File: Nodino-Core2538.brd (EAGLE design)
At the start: 27.9 x 25.4 mm, 21 parts, among them CON1 NODINO-JTAGMODULE, CON2 USB-OTG_SHIELD, IC1 CC2538, IC2 AP733333SAG, Q1 32MHz, Q2 32.768kHz

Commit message: final version, but still missing A0-A5 and AREF
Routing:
- net +3V3: track 83.3 -> 88.6 mm
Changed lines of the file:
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@@
 <via x="8.128" y="15.3035" extent="1-16" drill="0.3302"/>
 <wire x1="9.144" y1="9.0805" x2="10.3505" y2="10.287" width="0.2032" layer="16"/>
-<wire x1="10.3505" y1="10.287" x2="10.3505" y2="11.8745" width="0.2032" layer="16"/>
 <via x="10.414" y="11.938" extent="1-16" drill="0.3302"/>
 <wire x1="12.153384375" y1="12.278528125" x2="11.7954125" y2="12.6365" width="0.2032" layer="1"/>
 <wire x1="11.7954125" y1="12.6365" x2="11.1125" y2="12.6365" width="0.2032" layer="1"/>
 <wire x1="11.1125" y1="12.6365" x2="10.414" y2="11.938" width="0.2032" layer="1"/>
-<wire x1="10.3505" y1="11.8745" x2="10.414" y2="11.938" width="0.2032" layer="16"/>
 <wire x1="5.7785" y1="15.3035" x2="8.128" y2="15.3035" width="0.2032" layer="16"/>
 <wire x1="18.161" y1="17.526" x2="12.573" y2="11.938" width="0.2032" layer="16"/>
@@
 <wire x1="16.58466875" y1="16.52116875" x2="17.5895" y2="17.526" width="0.2032" layer="1"/>
 <wire x1="17.5895" y1="17.526" x2="18.2245" y2="17.526" width="0.2032" layer="1"/>
-<wire x1="6.096" y1="13.589" x2="5.2705" y2="12.7635" width="0.2032" layer="16"/>
+<wire x1="6.1595" y1="13.6525" x2="5.2705" y2="12.7635" width="0.2032" layer="16"/>
 <wire x1="5.2705" y1="12.7635" x2="4.2545" y2="12.7635" width="0.2032" layer="16"/>
 <wire x1="4.2545" y1="12.7635" x2="3.7465" y2="13.2715" width="0.2032" layer="16"/>
@@
 <wire x1="7.278" y1="15.152" x2="7.4295" y2="15.3035" width="0.2032" layer="1"/>
 <wire x1="7.4295" y1="15.3035" x2="8.128" y2="15.3035" width="0.2032" layer="1"/>
-<wire x1="10.414" y1="11.938" x2="7.278" y2="14.351" width="0" layer="19" extent="1-1"/>
+<wire x1="10.3505" y1="10.287" x2="10.3505" y2="11.049" width="0.2032" layer="16"/>
+<wire x1="10.3505" y1="11.049" x2="10.0965" y2="11.303" width="0.2032" layer="16"/>
+<wire x1="10.414" y1="11.938" x2="10.0965" y2="11.6205" width="0.2032" layer="16"/>
+<wire x1="10.0965" y1="11.6205" x2="10.0965" y2="11.303" width="0.2032" layer="16"/>
+<wire x1="10.414" y1="11.938" x2="9.652" y2="12.7" width="0.2032" layer="16"/>
+<wire x1="9.652" y1="12.7" x2="9.0805" y2="12.7" width="0.2032" layer="16"/>
+<wire x1="9.0805" y1="12.7" x2="8.128" y2="13.6525" width="0.2032" layer="16"/>
+<wire x1="8.128" y1="13.6525" x2="6.1595" y2="13.6525" width="0.2032" layer="16"/>
 </signal>
 <signal name="CS2">
@@
 <contactref element="IC1" pad="2"/>
 <via x="6.0325" y="9.652" extent="1-16" drill="0.3302"/>
-<via x="9.398" y="10.922" extent="1-16" drill="0.3302"/>
+<via x="9.5885" y="10.922" extent="1-16" drill="0.3302"/>
 <wire x1="11.604915625" y1="9.9695" x2="12.153384375" y2="10.58146875" width="0.2032" layer="1"/>
 <wire x1="11.604915625" y1="9.9695" x2="10.795" y2="9.9695" width="0.2032" layer="1"/>
@@
 <wire x1="5.2705" y1="8.89" x2="6.0325" y2="9.652" width="0.2032" layer="1"/>
 <wire x1="6.0325" y1="9.652" x2="7.3025" y2="10.922" width="0.2032" layer="16"/>
-<wire x1="7.3025" y1="10.922" x2="9.398" y2="10.922" width="0.2032" layer="16"/>
-<wire x1="9.398" y1="10.922" x2="9.8425" y2="10.922" width="0.2032" layer="1"/>
+<wire x1="7.3025" y1="10.922" x2="9.5885" y2="10.922" width="0.2032" layer="16"/>
+<wire x1="9.5885" y1="10.922" x2="9.8425" y2="10.922" width="0.2032" layer="1"/>
 <wire x1="9.8425" y1="10.922" x2="10.795" y2="9.9695" width="0.2032" layer="1"/>
 </signal>
@@
 <wire x1="8.509" y1="14.4145" x2="5.461" y2="14.4145" width="0.2032" layer="16"/>
 <wire x1="5.461" y1="14.4145" x2="4.826" y2="13.7795" width="0.2032" layer="16"/>
-<wire x1="8.509" y1="14.4145" x2="9.9695" y2="12.954" width="0.2032" layer="16"/>
-<wire x1="9.9695" y1="12.954" x2="10.9855" y2="12.954" width="0.2032" layer="16"/>
-<wire x1="10.9855" y1="12.954" x2="11.2395" y2="12.7" width="0.2032" layer="16"/>
+<wire x1="8.509" y1="14.4145" x2="9.4615" y2="13.462" width="0.2032" layer="16"/>
+<wire x1="9.4615" y1="13.462" x2="10.4775" y2="13.462" width="0.2032" layer="16"/>
+<wire x1="10.4775" y1="13.462" x2="11.2395" y2="12.7" width="0.2032" layer="16"/>
 <wire x1="11.2395" y1="12.7" x2="12.192" y2="12.7" width="0.2032" layer="16"/>
 </signal>
@@
 <wire x1="8.3185" y1="14.0335" x2="5.969" y2="14.0335" width="0.2032" layer="16"/>
 <wire x1="5.969" y1="14.0335" x2="5.08" y2="13.1445" width="0.2032" layer="16"/>
-<wire x1="8.3185" y1="14.0335" x2="9.779" y2="12.573" width="0.2032" layer="16"/>
-<wire x1="9.779" y1="12.573" x2="10.795" y2="12.573" width="0.2032" layer="16"/>
-<wire x1="10.795" y1="12.573" x2="11.049" y2="12.319" width="0.2032" layer="16"/>
+<wire x1="8.3185" y1="14.0335" x2="9.271" y2="13.081" width="0.2032" layer="16"/>
+<wire x1="9.271" y1="13.081" x2="10.287" y2="13.081" width="0.2032" layer="16"/>
+<wire x1="10.287" y1="13.081" x2="11.049" y2="12.319" width="0.2032" layer="16"/>
 <wire x1="11.049" y1="12.319" x2="12.3825" y2="12.319" width="0.2032" layer="16"/>
 </signal>

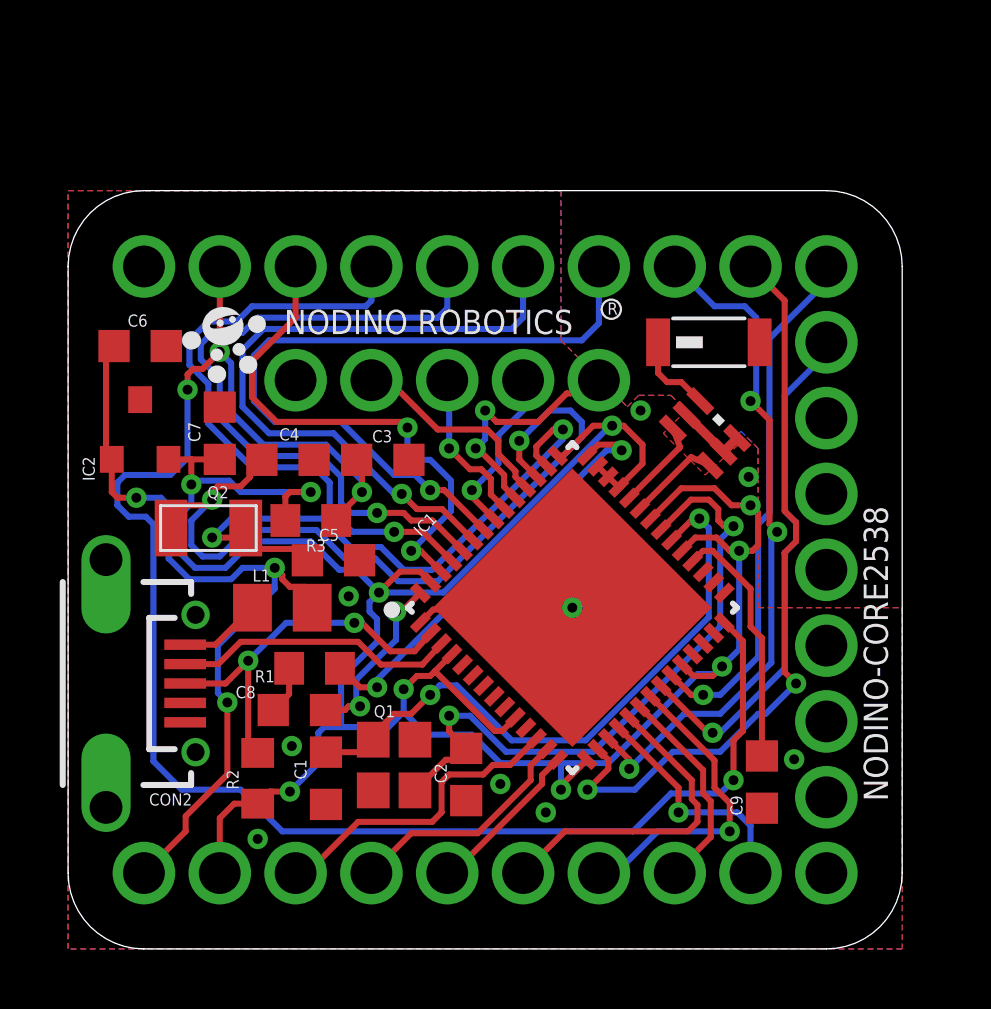
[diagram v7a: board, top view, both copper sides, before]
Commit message: added D15-D17
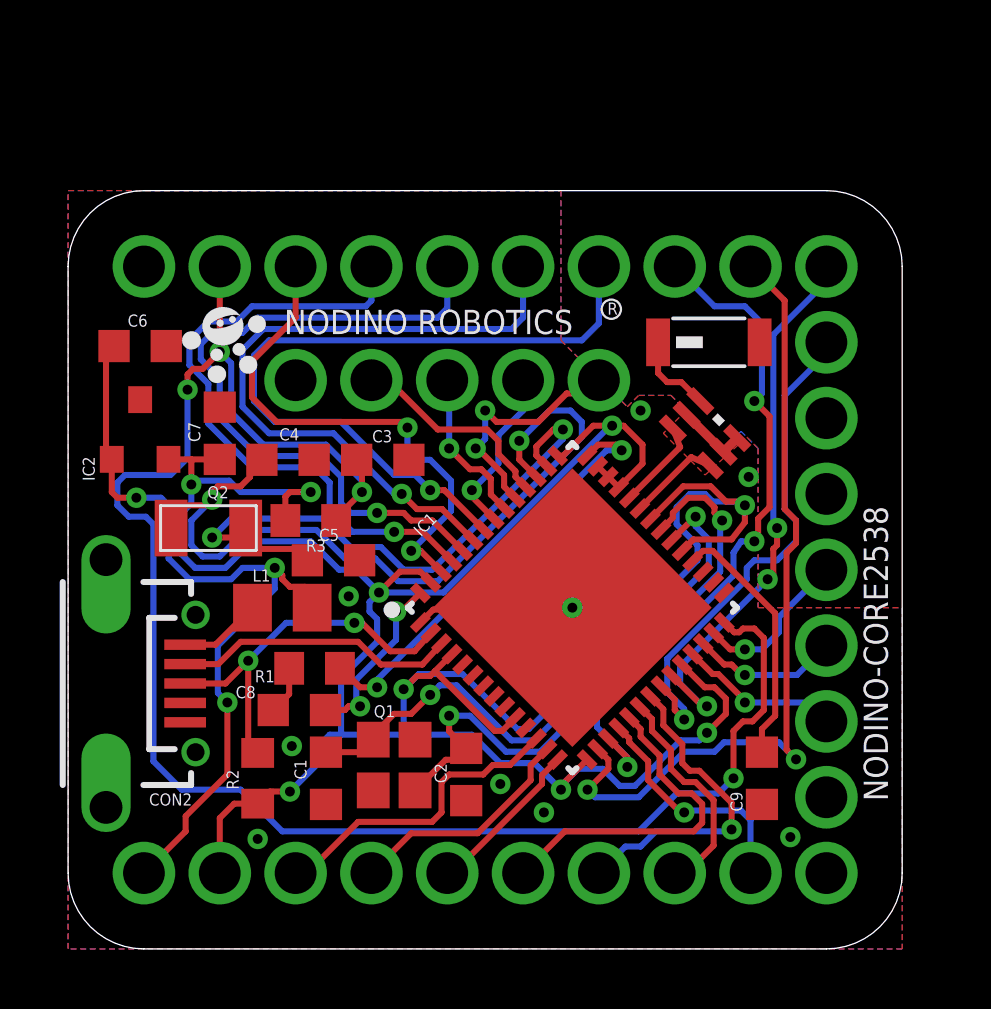
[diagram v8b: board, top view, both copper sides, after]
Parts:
- moved C9 0.13 mm to (23.2, 5.71)
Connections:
- new net PD0: CON1.12, IC1.25
- new net PD1: CON1.13, IC1.26
- new net PD2: CON1.14, IC1.27
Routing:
- net +3V3: track 88.6 -> 101.7 mm, vias 10 -> 9
- net PD0: track 0.00 -> 5.45 mm, vias 0 -> 1
- net PD2: track 0.00 -> 5.40 mm, vias 0 -> 1
- net PD1: track 0.00 -> 4.97 mm, vias 0 -> 1
- net UART_RX: track 25.2 -> 27.3 mm
- net N$7: track 21.9 -> 20.5 mm
- net NRST: track 57.1 -> 58.4 mm
- net PA7: track 17.7 -> 18.9 mm, vias 1 -> 3
- net N$8: track 21.0 -> 20.0 mm
- net SPI_MISO: track 7.05 -> 7.57 mm
- net SPI_NSS: track 11.0 -> 11.5 mm
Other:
- board text removed: "A0"
- board text removed: "A1"
- board text removed: "A2"
- board text removed: "A3"
- board text removed: "A4"
- board text removed: "A5"
- board text removed: "AREF"
- board text removed: "CAN"
- board text removed: "D14"
- board text removed: "D18"
- board text removed: "D19"
- board text removed: "SMB"
